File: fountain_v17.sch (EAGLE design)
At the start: 125 parts, among them IC1 UA741CDT, IC10 VCNT2020, IC11 VCNT2020, IC12 SN74LV4051APWR, IC13 LM7805CT_NOPB, IC14 LD1117AV33, IC15 SN74LS04N, IC16 SN74LS04N, IC2 LM555D, IC3 4532N, IC4 VCNT2020, IC5 VCNT2020, IC6 VCNT2020, IC7 VCNT2020, IC8 VCNT2020, IC9 VCNT2020, Q1 FQP30N06L, Q10 FQP30N06L, Q11 FQP30N06L, Q12 FQP30N06L, Q14 FQP30N06L, Q15 FQP30N06L, Q16 FQP30N06L, Q17 FQP30N06L, Q18 FQP30N06L, Q19 FQP30N06L, Q2 FQP30N06L, Q20 FQP30N06L, Q21 FQP30N06L, Q22 FQP30N06L, Q23 FQP30N06L, Q24 FQP30N06L, Q25 FQP30N06L, Q26 FQP30N06L, Q27 FQP30N06L, Q29 FQP30N06L, Q3 FQP30N06L, Q4 FQP30N06L, Q5 FQP30N06L, Q6 FQP30N06L, Q7 FQP30N06L, Q8 FQP30N06L, Q9 FQP30N06L, U1 MC34063ADR

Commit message: Resistor values updated
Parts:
- removed R4, R5, R6, R7: (no value), rcl:R-US_R0805
- added R10, R12, R14, R16: (no value), rcl:R-EU_0204/7
- R19: value 4k -> 7.12k
- R20: value 3.3k -> 5.68k
- R21: value 3k -> 5.03k
- R22: value 2.4k -> 3.83k
- R23: value 1.9k -> 2.76k
- R24: value 1.6k -> 2.26k
- R25: value 1.2k -> 1.36k
- R26: value 1k -> 0.948k
- RB: value 5k -> 3k
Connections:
- net +12V: now also R10.2, R12.2, R14.2, R16.2; no longer R4.2, R5.2, R6.2, R7.2
- net N$1: now also R10.1; no longer R4.1
- net N$3: now also R12.1; no longer R5.1
- net N$5: now also R14.1; no longer R6.1
- net N$7: now also R16.1; no longer R7.1
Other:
- note added: "These european symbol resistors stand for the solenoids"

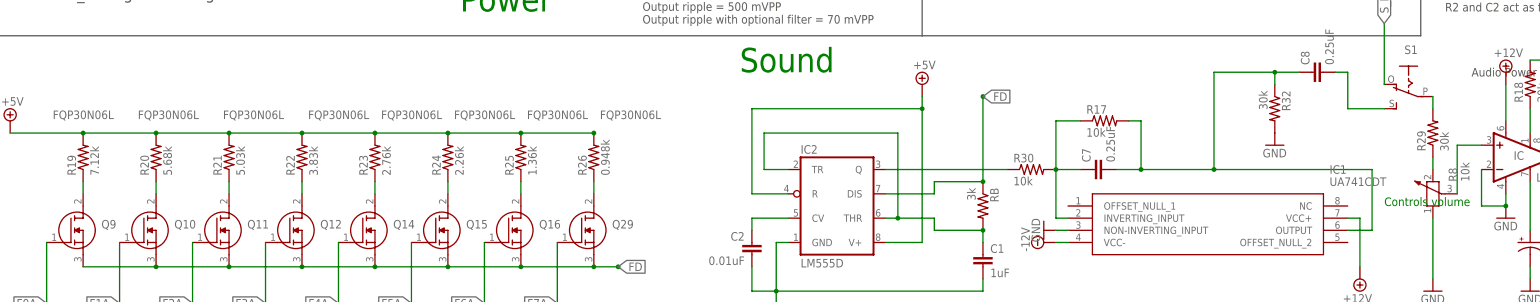
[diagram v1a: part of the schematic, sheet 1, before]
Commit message: Updated resistors
Updated all resistors, may be tested.
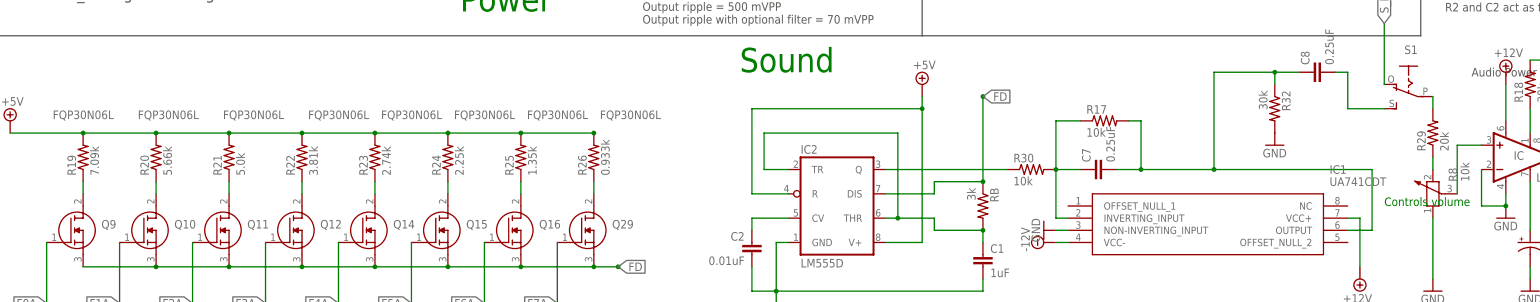
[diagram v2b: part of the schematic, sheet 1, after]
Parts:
- R19: value 7.12k -> 7.09k
- R20: value 5.68k -> 5.66k
- R21: value 5.03k -> 5.0k
- R22: value 3.83k -> 3.81k
- R23: value 2.76k -> 2.74k
- R24: value 2.26k -> 2.25k
- R25: value 1.36k -> 1.35k
- R26: value 0.948k -> 0.933k
- R29: value 30k -> 20k
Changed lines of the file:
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@@
 <part name="R15" library="rcl" library_urn="urn:adsk.eagle:library:334" deviceset="R-US_" device="R0805" package3d_urn="urn:adsk.eagle:package:23553/2" value="100k"/>
 <part name="SUPPLY1" library="supply2" library_urn="urn:adsk.eagle:library:372" deviceset="+12V" device=""/>
-<part name="R19" library="rcl" library_urn="urn:adsk.eagle:library:334" deviceset="R-US_" device="R0805" package3d_urn="urn:adsk.eagle:package:23553/2" value="7.12k"/>
-<part name="R20" library="rcl" library_urn="urn:adsk.eagle:library:334" deviceset="R-US_" device="R0805" package3d_urn="urn:adsk.eagle:package:23553/2" value="5.68k"/>
-<part name="R21" library="rcl" library_urn="urn:adsk.eagle:library:334" deviceset="R-US_" device="R0805" package3d_urn="urn:adsk.eagle:package:23553/2" value="5.03k"/>
-<part name="R22" library="rcl" library_urn="urn:adsk.eagle:library:334" deviceset="R-US_" device="R0805" package3d_urn="urn:adsk.eagle:package:23553/2" value="3.83k"/>
-<part name="R23" library="rcl" library_urn="urn:adsk.eagle:library:334" deviceset="R-US_" device="R0805" package3d_urn="urn:adsk.eagle:package:23553/2" value="2.76k"/>
-<part name="R24" library="rcl" library_urn="urn:adsk.eagle:library:334" deviceset="R-US_" device="R0805" package3d_urn="urn:adsk.eagle:package:23553/2" value="2.26k"/>
-<part name="R25" library="rcl" library_urn="urn:adsk.eagle:library:334" deviceset="R-US_" device="R0805" package3d_urn="urn:adsk.eagle:package:23553/2" value="1.36k"/>
-<part name="R26" library="rcl" library_urn="urn:adsk.eagle:library:334" deviceset="R-US_" device="R0805" package3d_urn="urn:adsk.eagle:package:23553/2" value="0.948k"/>
+<part name="R19" library="rcl" library_urn="urn:adsk.eagle:library:334" deviceset="R-US_" device="R0805" package3d_urn="urn:adsk.eagle:package:23553/2" value="7.09k"/>
+<part name="R20" library="rcl" library_urn="urn:adsk.eagle:library:334" deviceset="R-US_" device="R0805" package3d_urn="urn:adsk.eagle:package:23553/2" value="5.66k"/>
+<part name="R21" library="rcl" library_urn="urn:adsk.eagle:library:334" deviceset="R-US_" device="R0805" package3d_urn="urn:adsk.eagle:package:23553/2" value="5.0k"/>
+<part name="R22" library="rcl" library_urn="urn:adsk.eagle:library:334" deviceset="R-US_" device="R0805" package3d_urn="urn:adsk.eagle:package:23553/2" value="3.81k"/>
+<part name="R23" library="rcl" library_urn="urn:adsk.eagle:library:334" deviceset="R-US_" device="R0805" package3d_urn="urn:adsk.eagle:package:23553/2" value="2.74k"/>
+<part name="R24" library="rcl" library_urn="urn:adsk.eagle:library:334" deviceset="R-US_" device="R0805" package3d_urn="urn:adsk.eagle:package:23553/2" value="2.25k"/>
+<part name="R25" library="rcl" library_urn="urn:adsk.eagle:library:334" deviceset="R-US_" device="R0805" package3d_urn="urn:adsk.eagle:package:23553/2" value="1.35k"/>
+<part name="R26" library="rcl" library_urn="urn:adsk.eagle:library:334" deviceset="R-US_" device="R0805" package3d_urn="urn:adsk.eagle:package:23553/2" value="0.933k"/>
 <part name="IC" library="linear" library_urn="urn:adsk.eagle:library:262" deviceset="LM386?-*" device="M" package3d_urn="urn:adsk.eagle:package:16404/2" technology="1">
 <attribute name="SPICEPREFIX" value="X"/>
@@
 </part>
 <part name="R18" library="rcl" library_urn="urn:adsk.eagle:library:334" deviceset="R-US_" device="R0805" package3d_urn="urn:adsk.eagle:package:23553/2" value="30k"/>
-<part name="R29" library="rcl" library_urn="urn:adsk.eagle:library:334" deviceset="R-US_" device="R0805" package3d_urn="urn:adsk.eagle:package:23553/2" value="30k"/>
+<part name="R29" library="rcl" library_urn="urn:adsk.eagle:library:334" deviceset="R-US_" device="R0805" package3d_urn="urn:adsk.eagle:package:23553/2" value="20k"/>
 <part name="R32" library="rcl" library_urn="urn:adsk.eagle:library:334" deviceset="R-US_" device="R0805" package3d_urn="urn:adsk.eagle:package:23553/2" value="30k"/>
 <part name="C8" library="rcl" library_urn="urn:adsk.eagle:library:334" deviceset="C-EU" device="C0805" value="0.25uF">

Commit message: Tuning of resistors and aesthetic edits
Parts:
- R10, R12, R14, R16: value (none) -> 37.5
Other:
- note removed: "Audio Power Amplifier with Controlled Gain"
- note removed: "Bring one 5V cable into the upper part of the structure and one ground cable"
- moved on the sheet: Q1, Q2, Q3, Q4, Q5, Q6, Q7, Q8, R10, R12, R13, R14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

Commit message: updated resistors
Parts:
- R1: value 953R -> 953
- R3: value 0.24R -> 0.24
- RL1: value 100k -> 660
- RL2: value 100k -> 607
- RL3: value 100k -> 587

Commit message: Valves subcircuit changed
Using AND gates to control signal adds 1 extra digital output  from the microcontroller. The new circuit is in the top of the schametic.
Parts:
- added X1, X2, X3, X4, X5, X6, X7, X8: AND, ngspice-digital:AND
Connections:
- new net N$47: Q2.G, X5.Y
- new net N$48: Q1.G, X1.Y
- new net N$50: Q4.G, X6.Y
- new net N$51: Q3.G, X2.Y
- new net N$53: Q6.G, X7.Y
- new net N$54: Q5.G, X3.Y
- new net N$56: Q8.G, X8.Y
- new net N$57: Q7.G, X4.Y
- new net VALVE_ON: X1.B, X2.B, X3.B, X4.B, X5.B, X6.B, X7.B, X8.B
- net F0: now also X1.A
- net F0A: no longer Q1.G
- net F1: now also X5.A
- net F1A: no longer Q2.G
- net F2: now also X2.A
- net F2A: no longer Q3.G
- net F3: now also X6.A
- net F3A: no longer Q4.G
- net F4: now also X3.A
- net F4A: no longer Q5.G
- net F5: now also X7.A
- net F5A: no longer Q6.G
- net F6: now also X4.A
- net F6A: no longer Q7.G
- net F7: now also X8.A
- net F7A: no longer Q8.G
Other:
- note added: "Valve_ON comes from microcontroller"
- note removed: "These european symbol resistors stand for the solenoids"
- note removed: "These squares represent the valves"
- moved on the sheet: Q1, Q2, Q3, Q4, Q5, Q6, Q7, Q8, R10, R12, R13, R14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
